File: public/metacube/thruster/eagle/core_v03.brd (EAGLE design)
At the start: 30 x 49.2 mm, 0 parts

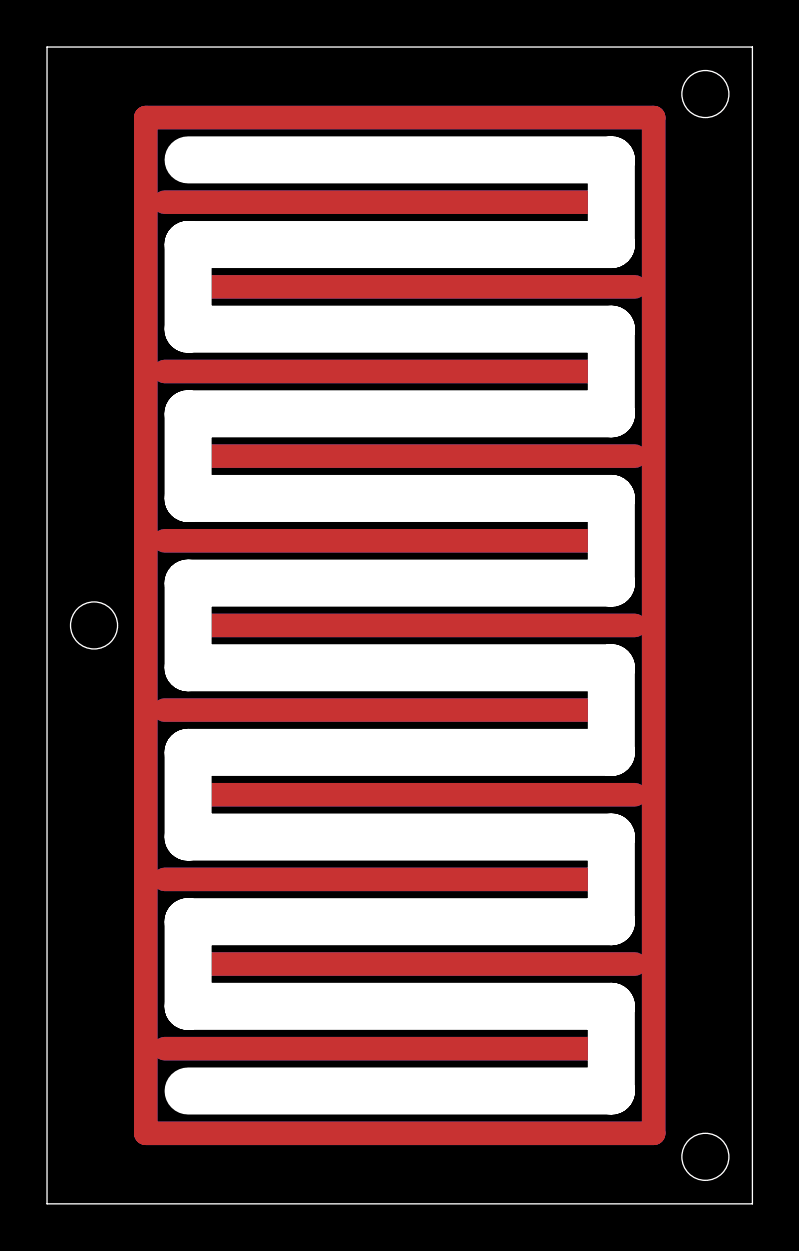
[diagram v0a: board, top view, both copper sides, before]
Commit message: 추력기 설계변경(댓글 김성현): 커버 랜드-히터 간섭 제거(랜드 끝 0.3 여유), 코어 슬롯 Milling→Dimension 폐곡선; EAGLE·뷰어·도면 갱신
Co-Authored-By: Claude Fable 5 <noreply@anthropic.com>
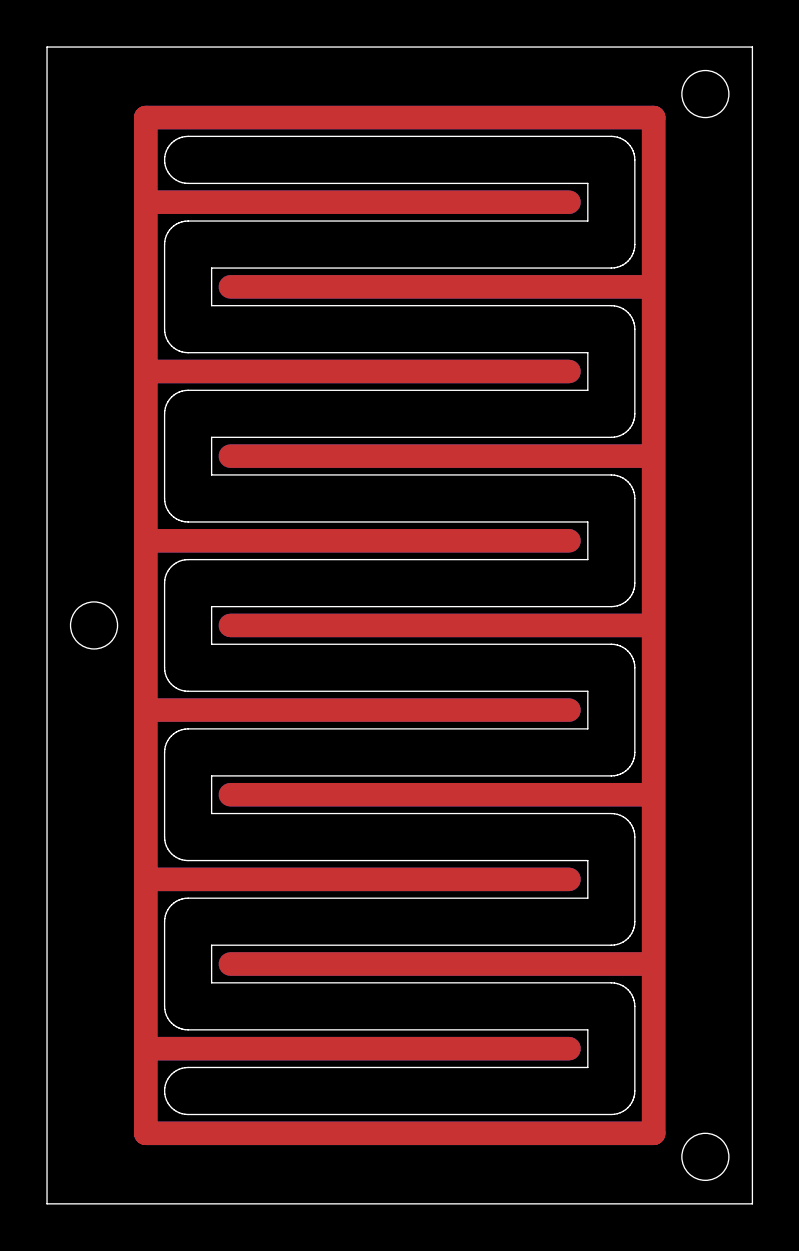
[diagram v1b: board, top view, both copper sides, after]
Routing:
- net LAND_TOP: track 327.6 -> 322.1 mm
- net LAND_BOT: track 327.6 -> 322.1 mm
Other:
- outline, holes or cut-outs redrawn
- board text added: "CORE FR-4 0.6mm 2L | slot = closed contour on Dimension L20 (2.0 wide, router 2.0, 12 passes, ~280 mm)"
- board text removed: "CORE FR-4 0.6mm 2L | slot=Milling L46 width 2.0 (router centreline, 12 passes, ~280 mm)"
